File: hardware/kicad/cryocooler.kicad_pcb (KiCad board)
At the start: 4 copper layers, 130 x 110 mm, 322 parts, among them J1 USB_C, J10 RTD PT1000 4-wire, J11 AMP OUT (+ / -), J12 CRYOCOOLER (+ / -), J13 COMPRESSOR RELAY / GND, J14 IMU LSM6DSOX module, J2 12V IN, J3 FAN (4-pin PWM), J4 PUMP (4-pin PWM), J5 ALPHACOOL ES FLOW (3-pin), J6 ALPHACOOL ES NTC 10k, J7 PANEL BUTTON, J8 AMP REM / GND, J9 AMP SIGNAL IN / GND, Q1 IRF4905S, Q10 BSS138, Q11 BSS138, Q12 BSS138, Q2 BSS138, Q3 BSS138, Q4 BSS138, Q5 BSS138, Q6 BSS84, Q7 BSS138, Q8 BSS84, Q9 BSS138, SW1 RESET, SW2 BOOT, SW3 POWER, U1 ESP32-S3-WROOM-2-N32R16V, U10 EMC2303-x-KP, U11 LTC2954CTS8-2, U12 LM4040DBZ-5, U13 CL25N8-G, U14 ADS1220IPW, U15 AP63205WU-7, U16 LD1117S33TR, U17 ISO7741DW, U18 ACS37800KMACTR-030B3-SPI, U2 USBLC6-2SC6, U20 ADP5071AREZ, U21 LT3097ADJC, U23 INA239AIDGSR, U24 74AHCT1G125, U25 SC18IS604PW, U26 74LVC1G125, U3 SG-8002CA-PH 25MHz, U4 AD9833BRMZ, U5 OPA1656ID, U6 AD633JRZ-R7, U7 MCP4921-E/SN, U8 LM4040DBZ-2.5, U9 OPA188ID

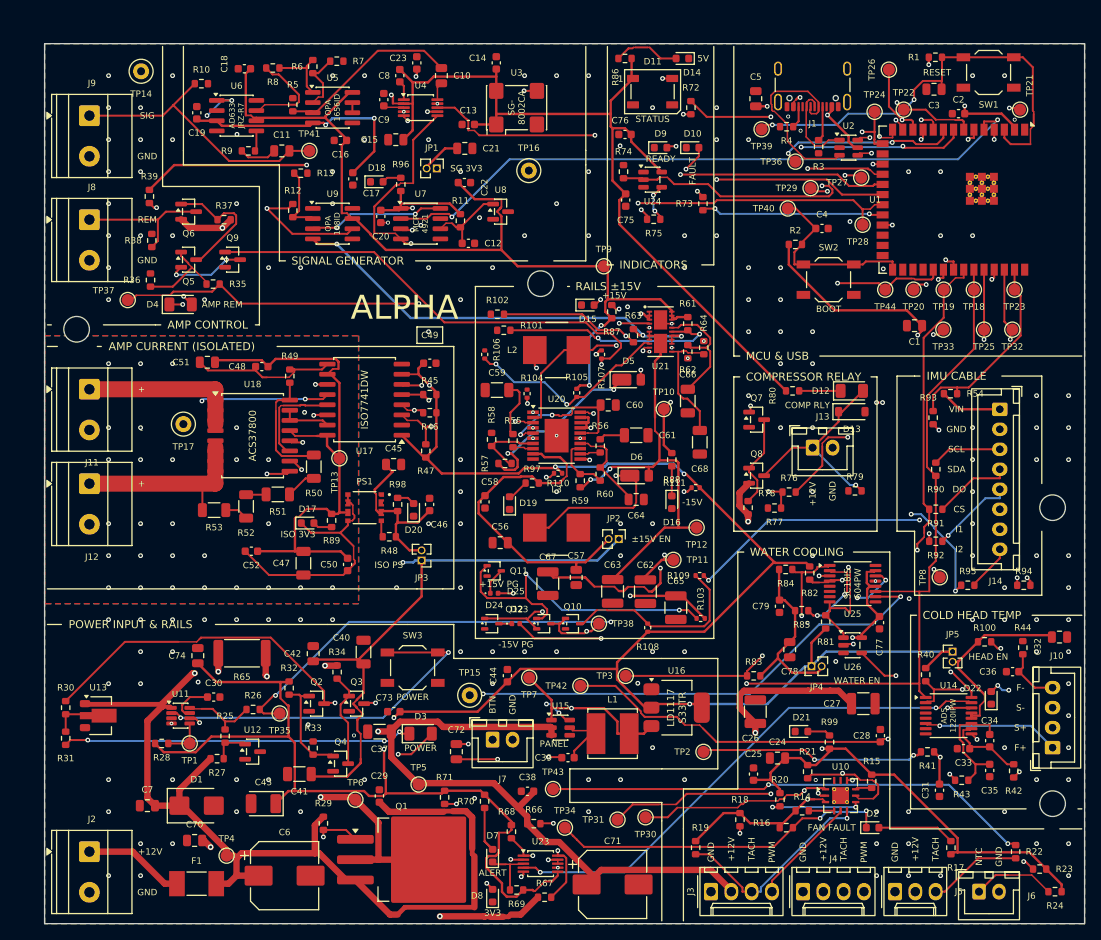
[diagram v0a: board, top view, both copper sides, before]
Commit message: WIP: restructure PCB for the Phoenix UCS 125-87 housing
Work in progress, layout not finished: about 90 parts still do not fit
their sections and the board is not routed.

- Right-angle connectors: Phoenix MSTBA 2,5 / MC 1,5, JST XH side entry,
  Hirose DF13, Molex 505448-0871 (new footprint from the Molex drawing)
- Datasheet and product links on every symbol (tools/part_links.py)
- Test points so every IC has one on its own nets
- gen_pcb.py: 100 x 62 mm two-sided board, housing holes and restricted
  corners, ESP32 antenna notch, one section per sheet, board ID block,
  ESP32 pin names, pin-1 marks, blue mask
- Housing drawings in hardware/housing/

Co-Authored-By: Claude Opus 5.5 <noreply@anthropic.com>
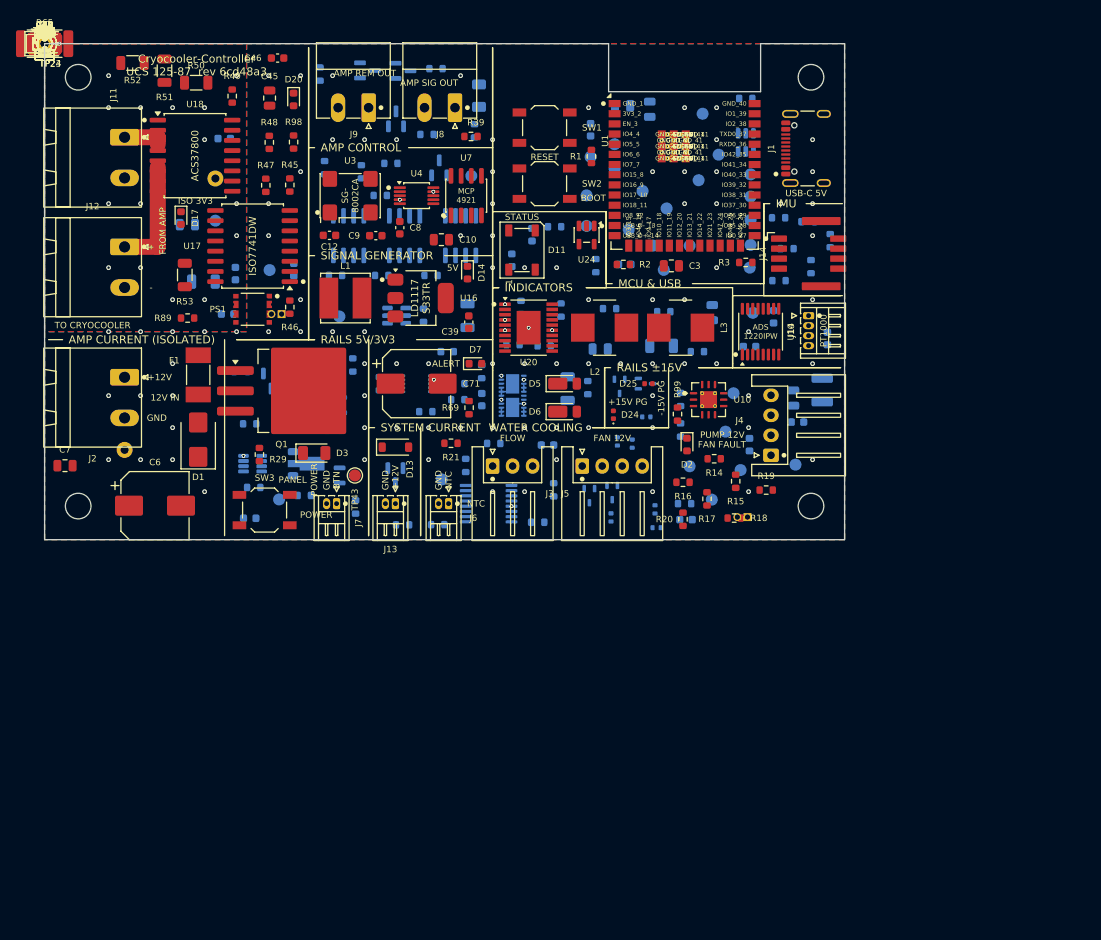
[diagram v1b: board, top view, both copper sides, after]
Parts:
- removed the ? at (126.0, 58.0)
- removed the ? at (62.0, 30.0)
- removed the ? at (4.00, 35.7)
- removed the ? at (126.0, 95.0)
- added ?: MountingHole_3.2mm_M3, MountingHole_3.2mm_M3, F.Cu at (95.8, 4.20)
- added ?: MountingHole_3.2mm_M3, MountingHole_3.2mm_M3, F.Cu at (4.20, 57.8)
- added ?: MountingHole_3.2mm_M3, MountingHole_3.2mm_M3, F.Cu at (4.20, 4.20)
- added ?: MountingHole_3.2mm_M3, MountingHole_3.2mm_M3, F.Cu at (95.8, 57.8)
- added TP45: AMP_REM_EN, TestPoint_Pad_D1.5mm, F.Cu at (0.00, 0.00)
- added TP46: PG_15V, TestPoint_Pad_D1.5mm, F.Cu at (0.00, 0.00)
- added TP47: ESP_EN, TestPoint_Pad_D1.5mm, B.Cu at (77.4, 28.3)
- added TP48: ESP_BOOT, TestPoint_Pad_D1.5mm, B.Cu at (77.7, 20.6)
- added TP49: SIG_SINE, TestPoint_Pad_D1.5mm, F.Cu at (0.00, 0.00)
- added TP50: NTC_ADC, TestPoint_Pad_D1.5mm, B.Cu at (83.4, 57.0)
- added TP51: FLOW_TACH, TestPoint_Pad_D1.5mm, B.Cu at (87.0, 53.3)
- added TP52: STATUS_RGB, TestPoint_Pad_D1.5mm, B.Cu at (67.8, 22.8)
- C1, C2, C24, C25, C26, C28, C30, C33, C34, C35, C37, C4, C47, C48, C49, C5, C50, C51, C52, C59, C60, C61, C64, C73, C77, D10, D21, D23, D4, D8, D9, JP3, JP4, Q10, Q11, Q12, Q2, Q3, Q4, Q5, Q6, Q8, Q9, R10, R103, R104, R105, R106, R107, R11, R111, R22, R23, R24, R25, R26, R27, R28, R30, R31, R32, R33, R35, R36, R37, R38, R4, R5, R54, R55, R56, R57, R58, R59, R6, R60, R61, R62, R63, R66, R67, R68, R7, R70, R71, R72, R73, R76, R8, R81, R82, R83, R84, R85, R86, R9, R90, R91, R92, R93, R94, U11, U12, U13, U15, U2, U21, U23, U25, U5, U6, U8, U9: moved to B.Cu
- J10: footprint JST_XH_B4B-XH-A_1x04_P2.50mm_Vertical -> Hirose_DF13-04P-1.25DS_1x04_P1.25mm_Horizontal
- J11, J12, J2: footprint TerminalBlock_Phoenix_MKDS-1,5-2-5.08_1x02_P5.08mm_Horizontal -> PhoenixContact_MSTBA_2,5_2-G-5,08_1x02_P5.08mm_Horizontal
- J13, J6, J7: footprint JST_XH_B2B-XH-A_1x02_P2.50mm_Vertical -> Hirose_DF13-02P-1.25DS_1x02_P1.25mm_Horizontal
- J14: footprint JST_XH_B8B-XH-A_1x08_P2.50mm_Vertical -> Molex_Micro-Lock_Plus_505448-0871_2x04_P1.25mm_Horizontal
- J3, J4: footprint Molex_KK-254_AE-6410-04A_1x04_P2.54mm_Vertical -> JST_XH_S4B-XH-A_1x04_P2.50mm_Horizontal
- J5: footprint Molex_KK-254_AE-6410-03A_1x03_P2.54mm_Vertical -> JST_XH_S3B-XH-A_1x03_P2.50mm_Horizontal
- J8, J9: footprint TerminalBlock_Phoenix_MKDS-1,5-2-5.08_1x02_P5.08mm_Horizontal -> PhoenixContact_MC_1,5_2-G-3.81_1x02_P3.81mm_Horizontal
- TP1: value LTC2954_INT -> USB_VBUS; moved to B.Cu
- TP10: value -15V -> +5V; moved to B.Cu
- TP11: value +16V5 -> +3V3
- TP12: value -16V5 -> +15V
- TP13: value ISO_3V3 -> -15V
- TP14: value GND -> +16V5; footprint TestPoint_Loop_D2.50mm_Drill1.0mm -> TestPoint_Pad_D1.5mm
- TP15: value GND -> -16V5; footprint TestPoint_Loop_D2.50mm_Drill1.0mm -> TestPoint_Pad_D1.5mm
- TP16: value GND -> ISO_3V3; footprint TestPoint_Loop_D2.50mm_Drill1.0mm -> TestPoint_Pad_D1.5mm; moved to B.Cu
- TP17: value ISO_GND -> +3V3_SG; footprint TestPoint_Loop_D2.50mm_Drill1.0mm -> TestPoint_Pad_D1.5mm
- TP18: value SPI_SCK -> +3V3_COOL; moved to B.Cu
- TP19: value SPI_MOSI -> +3V3_CH
- TP2: value ADS1220_DRDY -> MCP4921_VREF; moved to B.Cu
- TP20: value SPI_MISO -> +5V_PS15
- TP21: value MCP4921_CS -> +5V_ISO; moved to B.Cu
- TP22: value AD9833_FSYNC -> GND; footprint TestPoint_Pad_D1.5mm -> TestPoint_Loop_D2.50mm_Drill1.0mm; moved to B.Cu
- TP23: value IMU_CS -> GND; footprint TestPoint_Pad_D1.5mm -> TestPoint_Loop_D2.50mm_Drill1.0mm
- TP24: value INA239_CS -> GND; footprint TestPoint_Pad_D1.5mm -> TestPoint_Loop_D2.50mm_Drill1.0mm
- TP25: value ADS1220_CS -> ISO_GND; footprint TestPoint_Pad_D1.5mm -> TestPoint_Loop_D2.50mm_Drill1.0mm; moved to B.Cu
- TP26: value BRIDGE_CS -> SPI_SCK; moved to B.Cu
- TP27: value ACS_CS -> SPI_MOSI; moved to B.Cu
- TP28: value ACS_MISO -> SPI_MISO; moved to B.Cu
- TP29: value BRIDGE_RESET -> MCP4921_CS; moved to B.Cu
- TP3: value BRIDGE_INT -> LM4040_5V; moved to B.Cu
- TP30: value SDA -> AD9833_FSYNC; moved to B.Cu
- TP31: value SCL -> IMU_CS; moved to B.Cu
- TP32: value IMU_INT1 -> INA239_CS; moved to B.Cu
- TP33: value IMU_INT2 -> ADS1220_CS; moved to B.Cu
- TP34: value FAN_ALERT -> BRIDGE_CS; moved to B.Cu
- TP35: value PWR_KILL -> ACS_CS; moved to B.Cu
- TP36: value COMP_RELAY_EN -> ACS_MISO; moved to B.Cu
- TP37: value AMP_REM_EN -> BRIDGE_RESET; moved to B.Cu
- TP38: value PG_15V -> SDA; moved to B.Cu
- TP39: value ESP_EN -> SCL; moved to B.Cu
- TP4: value VIN -> LTC2954_INT; moved to B.Cu
- TP40: value ESP_BOOT -> IMU_INT1; moved to B.Cu
- TP41: value SIG_SINE -> IMU_INT2; moved to B.Cu
- TP42: value NTC_ADC -> FAN_ALERT; moved to B.Cu
- TP43: value FLOW_TACH -> PWR_KILL
- TP44: value STATUS_RGB -> COMP_RELAY_EN; moved to B.Cu
- TP5: value +12V -> ADS1220_DRDY; moved to B.Cu
- TP6: value VSW -> BRIDGE_INT; moved to B.Cu
- TP7: value +5V -> VIN; moved to B.Cu
- TP8: value +3V3 -> +12V
- TP9: value +15V -> VSW
- moved R42 151.5 mm to (0.00, 0.00), turned to 0 degrees
- moved R43 147.0 mm to (0.00, 0.00), turned to 0 degrees
- moved C32 147.0 mm to (0.00, 0.00)
- moved C31 145.7 mm to (0.00, 0.00), turned to 0 degrees
- moved C36 144.2 mm to (0.00, 0.00), turned to 0 degrees
- moved D22 143.8 mm to (0.00, 0.00), turned to 0 degrees
- moved R44 143.7 mm to (0.00, 0.00), turned to 0 degrees
- moved R41 141.5 mm to (0.00, 0.00), turned to 0 degrees
- moved R100 139.3 mm to (0.00, 0.00)
- moved JP5 136.6 mm to (0.00, 0.00)
- moved R40 135.5 mm to (0.00, 0.00), turned to 0 degrees
- moved R95 133.8 mm to (0.00, 0.00)
- moved C27 131.5 mm to (0.00, 0.00)
- moved TP8 130.3 mm to (0.00, 0.00)
- moved U26 125.9 mm to (0.00, 0.00)
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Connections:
- TP1 pad 1: Net-(U11-~{INT}) -> /USB_VBUS
- TP10 pad 1: -15V -> +5V
- TP11 pad 1: +16V5 -> +3V3
- TP12 pad 1: -16V5 -> +15V
- TP13 pad 1: ISO_3V3 -> -15V
- TP14 pad 1: GND -> +16V5
- TP15 pad 1: GND -> -16V5
- TP16 pad 1: GND -> ISO_3V3
- TP17 pad 1: ISO_GND -> +3V3_SG
- TP18 pad 1: SPI_SCK -> +3V3_COOL
- TP19 pad 1: SPI_MOSI -> +3V3_CH
- TP2 pad 1: Net-(U14-~{DRDY}) -> Net-(U7-Vref)
- TP20 pad 1: SPI_MISO -> +5V_PS15
- TP21 pad 1: MCP4921_CS -> +5V_ISO
- TP22 pad 1: AD9833_FSYNC -> GND
- TP23 pad 1: IMU_CS -> GND
- TP24 pad 1: INA239_CS -> GND
- TP25 pad 1: ADS1220_CS -> ISO_GND
- TP26 pad 1: BRIDGE_CS -> SPI_SCK
- TP27 pad 1: ACS_CS -> SPI_MOSI
- TP28 pad 1: ACS_MISO -> SPI_MISO
- TP29 pad 1: BRIDGE_RESET -> MCP4921_CS
- TP3 pad 1: /Water Cooling I2C Bridge/BRIDGE_INT -> Net-(U12-K)
- TP30 pad 1: SDA -> AD9833_FSYNC
- TP31 pad 1: SCL -> IMU_CS
- TP32 pad 1: IMU_INT1 -> INA239_CS
- TP33 pad 1: IMU_INT2 -> ADS1220_CS
- TP34 pad 1: FAN_ALERT -> BRIDGE_CS
- TP35 pad 1: PWR_KILL -> ACS_CS
- TP36 pad 1: COMP_RELAY_EN -> ACS_MISO
- TP37 pad 1: AMP_REM_EN -> BRIDGE_RESET
- TP38 pad 1: PG_15V -> SDA
- TP39 pad 1: ESP_EN -> SCL
- TP4 pad 1: VIN -> Net-(U11-~{INT})
- TP40 pad 1: ESP_BOOT -> IMU_INT1
- TP41 pad 1: SIG_SINE -> IMU_INT2
- TP42 pad 1: NTC_ADC -> FAN_ALERT
- TP43 pad 1: FLOW_TACH -> PWR_KILL
- TP44 pad 1: STATUS_RGB -> COMP_RELAY_EN
- TP5 pad 1: +12V -> Net-(U14-~{DRDY})
- TP6 pad 1: VSW -> /Water Cooling I2C Bridge/BRIDGE_INT
- TP7 pad 1: +5V -> VIN
- TP8 pad 1: +3V3 -> +12V
- TP9 pad 1: +15V -> VSW
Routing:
- net +3V3: track 482.0 -> 0.00 mm, vias 11 -> 0
- net +5V: track 316.1 -> 0.00 mm, vias 4 -> 0
- net +12V: track 310.7 -> 0.00 mm, vias 6 -> 0
- net SPI_SCK: track 234.1 -> 0.00 mm, vias 4 -> 0
- net SPI_MOSI: track 232.5 -> 0.00 mm, vias 6 -> 0
- net -15V: track 168.1 -> 1.00 mm, vias 8 -> 0
- net NTC_ADC: track 157.5 -> 0.00 mm, vias 2 -> 0
- net FLOW_TACH: track 157.0 -> 0.00 mm, vias 4 -> 0
- net +15V: track 152.9 -> 1.00 mm, vias 3 -> 0
- net +3V3_COOL: track 142.5 -> 0.00 mm, vias 3 -> 0
- net VIN: track 141.0 -> 0.00 mm, vias 2 -> 0
- net SPI_MISO: track 139.2 -> 0.00 mm, vias 6 -> 0
- net PWR_KILL: track 127.8 -> 0.00 mm, vias 3 -> 0
- net AMP_REM_EN: track 124.4 -> 0.00 mm, vias 2 -> 0
- net FAN_ALERT: track 121.6 -> 0.00 mm, vias 6 -> 0
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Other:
- board size 130 x 110 mm -> 100 x 62 mm
- board text added: "12V IN"
- board text added: "3V3_2"
- board text added: "AMP REM OUT"
- board text added: "AMP SIG OUT"
- board text added: "COLD HEAD"
- board text added: "Cryocooler-Controller"
- board text added: "EN_3"
- board text added: "FAN 12V"
- board text added: "FLOW"
- board text added: "FROM AMP"
- board text added: "GND_1"
- board text added: "GND_40"
- board text added: "GND_41"
- board text added: "I2C BRIDGE"
- board text added: "IMU"
- board text added: "IO0_27"
- board text added: "IO10_18"
- board text added: "IO11_19"
- board text added: "IO12_20"
- board text added: "IO13_21"
- board text added: "IO14_22"
- board text added: "IO15_8"
- board text added: "IO16_9"
- board text added: "IO17_10"
- board text added: "IO18_11"
- board text added: "IO1_39"
- board text added: "IO21_23"
- board text added: "IO2_38"
- board text added: "IO35_28"
- board text added: "IO36_29"
- board text added: "IO37_30"
- board text added: "IO38_31"
- board text added: "IO39_32"
- board text added: "IO3_15"
- board text added: "IO40_33"
- board text added: "IO41_34"
- board text added: "IO42_35"
- board text added: "IO45_26"
- board text added: "IO46_16"
- board text added: "IO47_24"
- board text added: "IO48_25"
- board text added: "IO4_4"
- board text added: "IO5_5"
- board text added: "IO6_6"
- board text added: "IO7_7"
- board text added: "IO8_12"
- board text added: "IO9_17"
- board text added: "PT1000"
- board text added: "PUMP 12V"
- board text added: "RAILS 5V/3V3"
- board text added: "RXD0_36"
- board text added: "SYSTEM CURRENT"
- board text added: "TO CRYOCOOLER"
- board text added: "TXD0_37"
- board text added: "UCS 125-87 rev 6cd48a3"
- board text added: "USB-C 5V"
- board text added: "USB_D+_14"
- board text added: "USB_D-_13"
- board text removed: "+15V"
- board text removed: "-15V"
- board text removed: "ALPHA"
- board text removed: "ALPHA DEV UNIT"
- board text removed: "COLD HEAD TEMP"
- board text removed: "COMP RLY"
- board text removed: "COMPRESSOR RELAY"
- board text removed: "CS"
- board text removed: "DO"
- board text removed: "F+"
- board text removed: "F-"
- board text removed: "HEAD EN"
- board text removed: "I1"
- board text removed: "I2"
- board text removed: "IMU CABLE"
- board text removed: "POWER INPUT & RAILS"
- board text removed: "PWM"
- board text removed: "REM"
- board text removed: "S+"
- board text removed: "S-"
- board text removed: "SCL"
- board text removed: "SDA"
- board text removed: "SG 3V3"
- board text removed: "SIG"
- board text removed: "STI Hybrid-98 Cryocooler Control Unit"
- board text removed: "TACH"
- board text removed: "VIN"
- board text removed: "±15V EN"

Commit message: WIP: pack the UCS 125-87 board and enforce readable silkscreen
Placement on the 100 x 62 mm board now gets every part on with the
silkscreen check passing in most runs, but the board is at capacity and
not yet stable or routed. Generator changes:

- grid index for the occupancy map (about 4x faster placement)
- through-hole parts checked against the other side, placed first
- largest parts first, test points last, 0.25 mm retry grid
- text measured with pcbnew; silk check also flags text over pads
- vertical and in-box section titles, short title and label forms
- connector pin and function labels reserved early, other-side fallback
- references with no room hidden from silkscreen (kept on Fab)
- AGENTS.md: readable-silkscreen and every-part-placed directives

Co-Authored-By: Claude Opus 5.5 <noreply@anthropic.com>
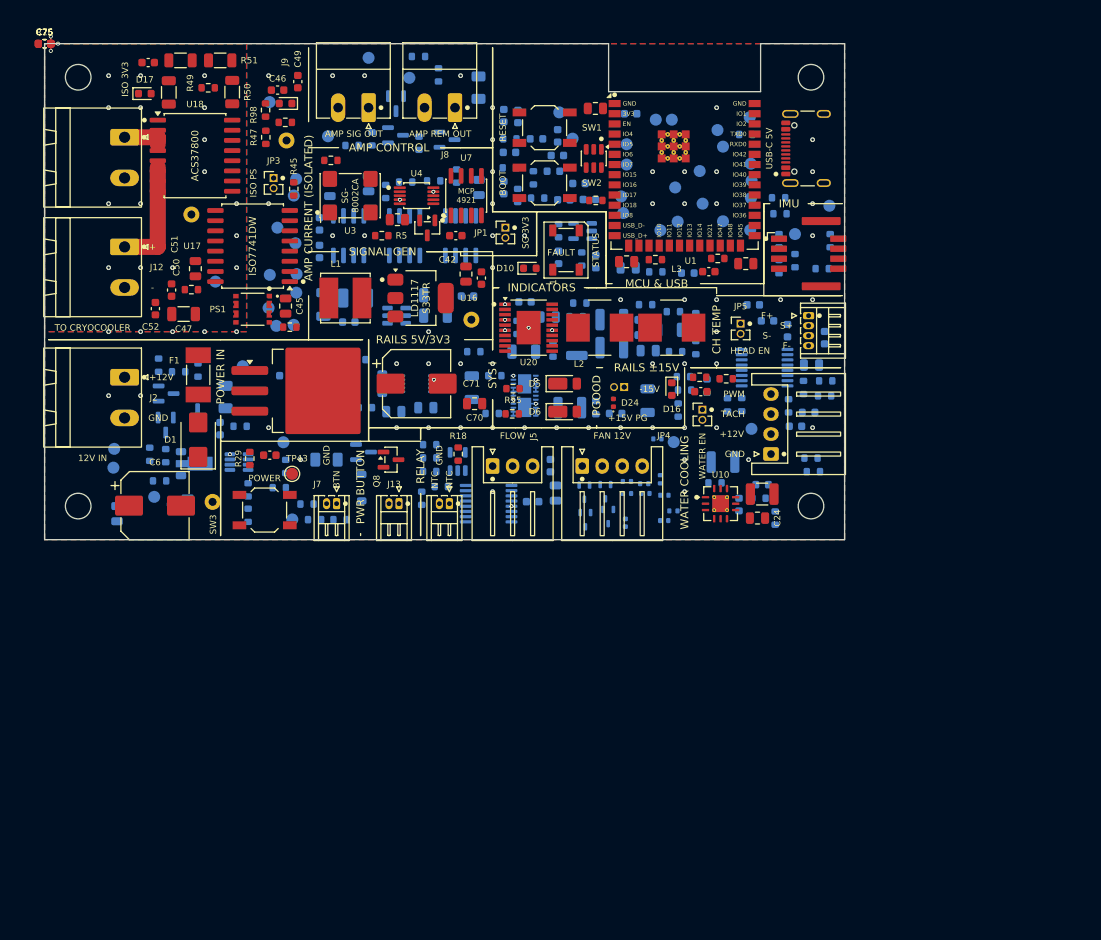
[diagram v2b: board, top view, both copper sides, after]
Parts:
- C1, C24, C25, C26, C28, C4, C47, C48, C49, C5, C50, C51, C52, D10, JP3, JP4, Q8, R11, R5, R55, R56, U2, U8: moved to F.Cu
- C11, C12, C13, C14, C15, C16, C17, C18, C19, C20, C21, C22, C23, C27, C31, C32, C36, C38, C39, C40, C41, C43, C56, C57, C58, C62, C63, C65, C66, C67, C68, C7, C72, C74, C78, C79, C9, D12, D13, D14, D15, D18, D19, D2, D22, D25, D3, D7, JP2, Q7, R100, R101, R102, R108, R109, R110, R12, R13, R16, R17, R19, R20, R21, R34, R39, R40, R41, R42, R43, R44, R64, R65, R69, R74, R77, R78, R79, R80, R87, R88, R95, R96, R97, R99, TP11, TP12, TP13, TP14, TP15, TP17, TP19, TP20, TP23, TP24, TP45, TP46, TP49, TP8, TP9, U14, U24, U26: moved to B.Cu
- moved R44 107.0 mm to (97.5, 44.0)
- moved R42 106.3 mm to (97.6, 42.1)
- moved D22 106.0 mm to (95.5, 46.1), turned to 180 degrees
- moved C31 105.3 mm to (93.9, 47.8)
- moved C25 105.3 mm to (0.00, 0.00)
- moved C36 104.2 mm to (97.5, 36.8), turned to 90 degrees
- moved R41 104.1 mm to (94.9, 43.0), turned to 90 degrees
- moved C32 103.9 mm to (95.9, 40.2)
- moved R100 103.4 mm to (93.0, 45.3), turned to -90 degrees
- moved R95 101.2 mm to (97.2, 28.1)
- moved C27 99.6 mm to (84.8, 52.3), turned to 180 degrees
- moved R40 98.1 mm to (87.1, 45.1), turned to 90 degrees
- moved R43 96.6 mm to (85.4, 45.1), turned to -90 degrees
- moved R108 95.9 mm to (77.5, 56.5), turned to 180 degrees
- moved R109 94.3 mm to (77.0, 54.5), turned to 90 degrees
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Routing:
- net GND: track 1.74 -> 3.54 mm, vias 123 -> 90
- net ISO_GND: vias 20 -> 21
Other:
- board text added: "+/-"
- board text added: "+15V"
- board text added: "-15V"
- board text added: "CH TEMP"
- board text added: "COMP RELAY"
- board text added: "COMP RLY"
- board text added: "DO/CS"
- board text added: "EN"
- board text added: "F+"
- board text added: "F-"
- board text added: "HEAD EN"
- board text added: "I1/I2"
- board text added: "IO1"
- board text added: "IO10"
- board text added: "IO11"
- board text added: "IO12"
- board text added: "IO13"
- board text added: "IO14"
- board text added: "IO15"
- board text added: "IO16"
- board text added: "IO17"
- board text added: "IO18"
- board text added: "IO2"
- board text added: "IO21"
- board text added: "IO36"
- board text added: "IO37"
- board text added: "IO38"
- board text added: "IO39"
- board text added: "IO4"
- board text added: "IO40"
- board text added: "IO41"
- board text added: "IO42"
- board text added: "IO45"
- board text added: "IO47"
- board text added: "IO48"
- board text added: "IO5"
- board text added: "IO6"
- board text added: "IO7"
- board text added: "IO8"
- board text added: "PGOOD"
- board text added: "POWER BUTTON"
- board text added: "POWER GOOD"
- board text added: "POWER IN"
- board text added: "PWM"
- board text added: "PWR BUTTON"
- board text added: "RELAY"
- board text added: "RELAY 12V OUT"
- board text added: "REM"
- board text added: "RXD0"
- board text added: "S+"
- board text added: "S-"
- board text added: "SCL/SDA"
- board text added: "SG 3V3"
- board text added: "SIG"
- board text added: "SIGNAL GEN"
- board text added: "SYS I"
- board text added: "TACH"
- board text added: "TXD0"
- board text added: "UCS 125-87 rev 427bca0"
- board text added: "USB_D+"
- board text added: "USB_D-"
- board text added: "VIN/GND"
- board text added: "WATER"
- board text added: "±15V EN"
- board text removed: "3V3_2"
- board text removed: "EN_3"
- board text removed: "GND_1"
- board text removed: "GND_40"
- board text removed: "GND_41"
- board text removed: "IO0_27"
- board text removed: "IO10_18"
- board text removed: "IO11_19"
- board text removed: "IO12_20"
- board text removed: "IO13_21"
- board text removed: "IO14_22"
- board text removed: "IO15_8"
- board text removed: "IO16_9"
- board text removed: "IO17_10"
- board text removed: "IO18_11"
- board text removed: "IO1_39"
- board text removed: "IO21_23"
- board text removed: "IO2_38"
- board text removed: "IO35_28"
- board text removed: "IO36_29"
- board text removed: "IO37_30"
- board text removed: "IO38_31"
- board text removed: "IO39_32"
- board text removed: "IO3_15"
- board text removed: "IO40_33"
- board text removed: "IO41_34"
- board text removed: "IO42_35"
- board text removed: "IO45_26"
- board text removed: "IO46_16"
- board text removed: "IO47_24"
- board text removed: "IO48_25"
- board text removed: "IO4_4"
- board text removed: "IO5_5"
- board text removed: "IO6_6"
- board text removed: "IO7_7"
- board text removed: "IO8_12"
- board text removed: "IO9_17"
- board text removed: "RXD0_36"
- board text removed: "SYSTEM CURRENT"
- board text removed: "TXD0_37"
- board text removed: "UCS 125-87 rev 6cd48a3"
- board text removed: "USB_D+_14"
- board text removed: "USB_D-_13"
